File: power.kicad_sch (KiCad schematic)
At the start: 71 parts, among them SW1 SW_Push, U3 BD71847MWV, Y1 Crystal

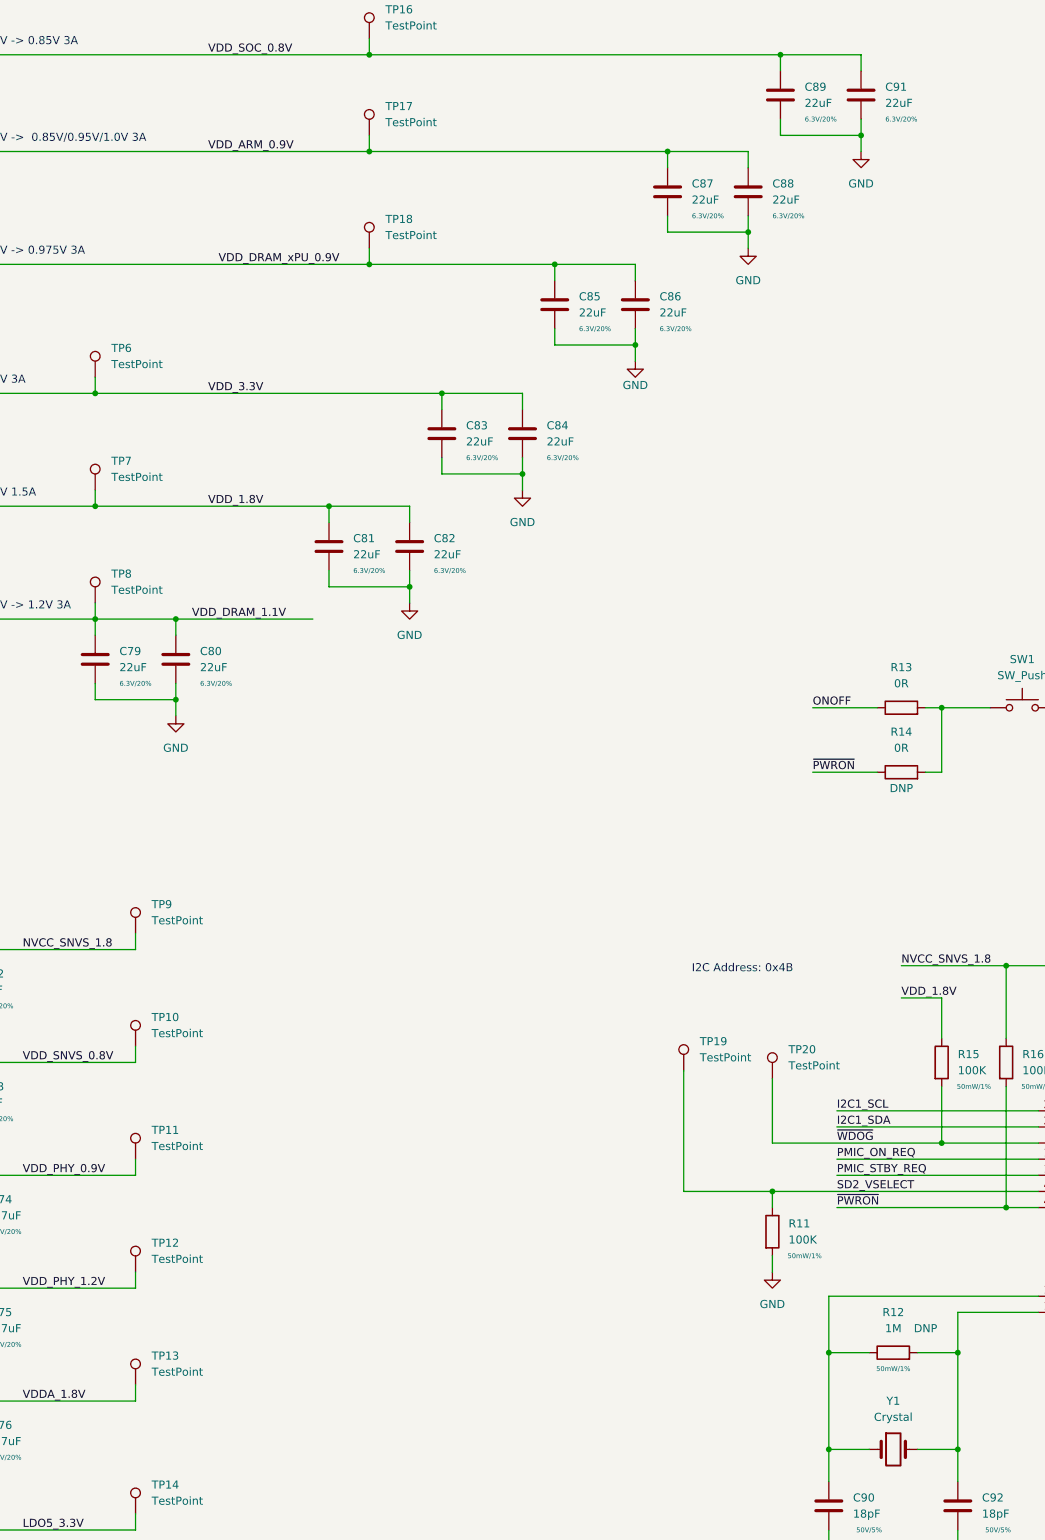
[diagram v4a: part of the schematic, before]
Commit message: bom work, change uart level shifter and m.2 socket
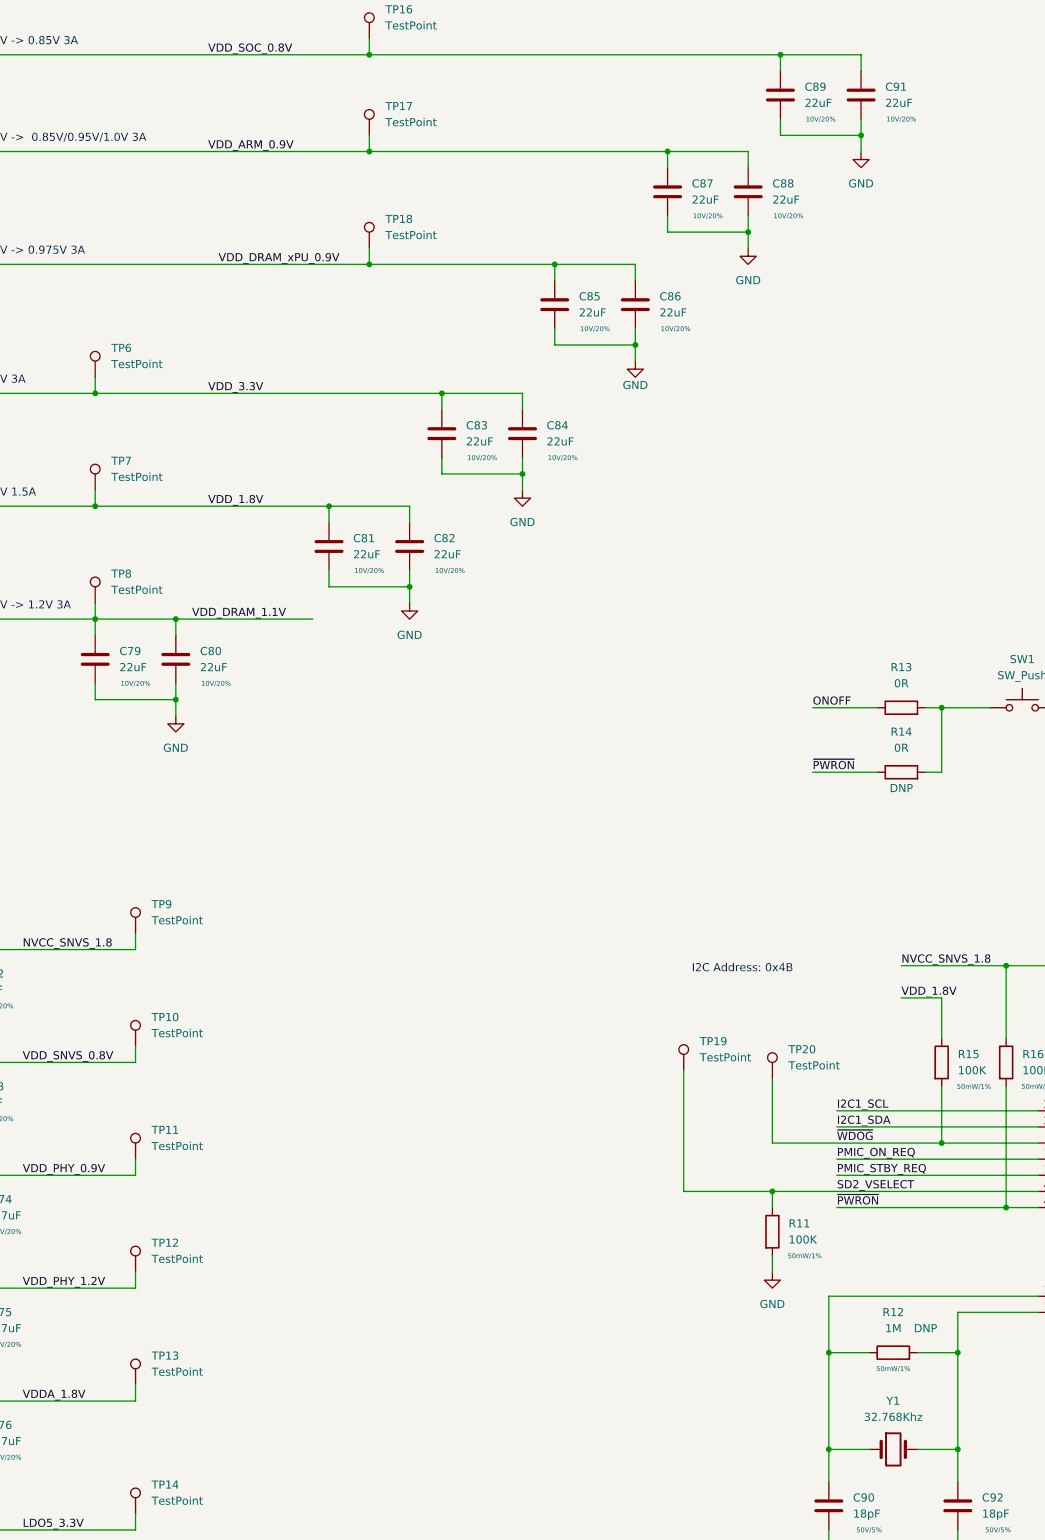
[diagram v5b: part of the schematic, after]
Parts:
- C58, C59, C60: MPN (none) -> GRM155C81C225ME15D
- C61, C62, C63, C74, C75, C76, C77: MPN (none) -> CL05A475MP5NRNC
- C64, C65, C66, C67, C68, C69, C70, C71, C78: MPN (none) -> CL10A106KP8NNNC
- C72, C73, C93, C94: MPN (none) -> CL05A105KP5NNNC
- C79, C80, C81, C82, C83, C84, C85, C86, C87, C88, C89, C91: MPN (none) -> CL10A226MP8NUNE; Rating 6.3V/20% -> 10V/20%
- C90, C92: footprint qsbc:C_0402_1005Metric -> qsbc:C_0201_0603Metric; MPN (none) -> GRM0335C1H180JA01D
- L1, L2, L3, L5, L6: MPN (none) -> DFE252012P-R47M=P2
- L4: MPN (none) -> DFE252012P-1R0M=P2
- R11, R15, R16: MPN (none) -> RC0402FR-07100KL
- R12: MPN (none) -> RC0402FR-071ML
- R13, R14: MPN (none) -> RC0402FR-070RL
- SW1: MPN (none) -> EVQ-P7A01P
- U3: MPN (none) -> BD71847AMWV-E2
- Y1: value Crystal -> 32.768Khz; MPN (none) -> ECS-.327-12.5-12R-C-TR

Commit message: ddr length matching work, misc cleanup
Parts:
- renumbered C58 to C57, C59 to C58, C60 to C59, C61 to C60, C62 to C61, C63 to C62, C64 to C63, C65 to C64, C66 to C65, C67 to C66, C68 to C67, C69 to C68, C70 to C69, C71 to C70, C72 to C71, C73 to C72, C74 to C73, C75 to C74, C76 to C75, C77 to C76, C78 to C77, C79 to C78, C80 to C79, C81 to C80, C82 to C81, C83 to C82, C84 to C83, C85 to C84, C86 to C85, C87 to C86, C88 to C87, C89 to C88, C90 to C89, C91 to C90, C92 to C91, C93 to C92, C94 to C93

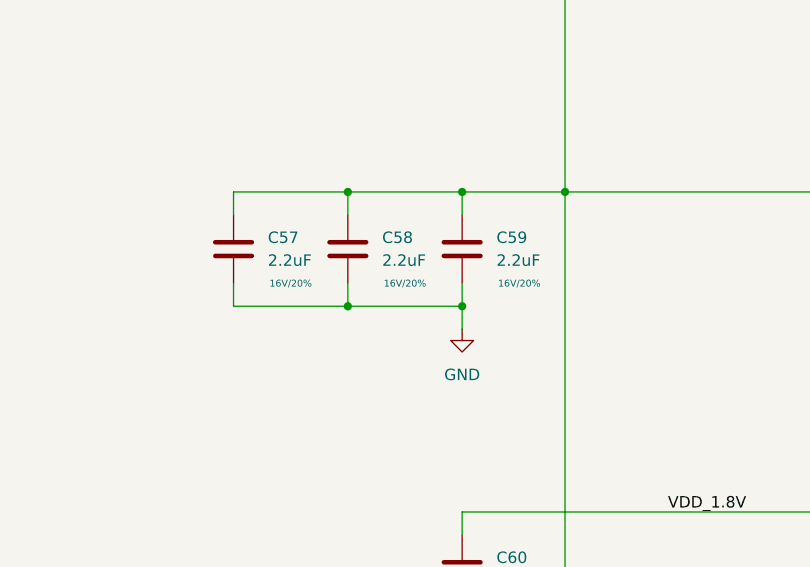
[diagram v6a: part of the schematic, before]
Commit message: misc cleanup, change from usb mux to dual uart
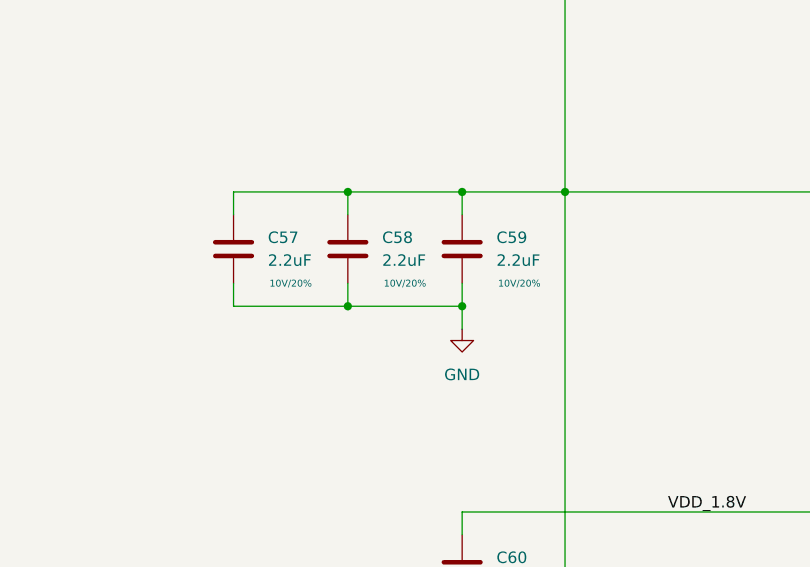
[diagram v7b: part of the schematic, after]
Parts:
- C57, C58, C59: MPN GRM155C81C225ME15D -> GRM155R61A225KE95D; Rating 16V/20% -> 10V/20%
- TP10, TP11, TP12, TP13, TP14, TP15, TP16, TP17, TP18, TP19, TP2, TP20, TP3, TP4, TP5, TP6, TP7, TP8, TP9: now left out of the parts list
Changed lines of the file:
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@@
   )
   (symbol (lib_id "Connector:TestPoint") (at 257.81 49.53 0) (unit 1)
-    (in_bom yes) (on_board yes) (fields_autoplaced)
+    (in_bom no) (on_board yes) (fields_autoplaced)
     (property "Reference" "TP16" (id 0) (at 260.35 44.9579 0)
       (effects (font (size 1.27 1.27)) (justify left))
@@
   )
   (symbol (lib_id "Connector:TestPoint") (at 73.66 381 0) (unit 1)
-    (in_bom yes) (on_board yes) (fields_autoplaced)
+    (in_bom no) (on_board yes) (fields_autoplaced)
     (property "Reference" "TP4" (id 0) (at 76.2 376.4279 0)
       (effects (font (size 1.27 1.27)) (justify left))
@@
   )
   (symbol (lib_id "Connector:TestPoint") (at 220.98 281.94 0) (unit 1)
-    (in_bom yes) (on_board yes) (fields_autoplaced)
+    (in_bom no) (on_board yes) (fields_autoplaced)
     (property "Reference" "TP14" (id 0) (at 223.52 277.3679 0)
       (effects (font (size 1.27 1.27)) (justify left))
@@
   )
   (symbol (lib_id "Connector:TestPoint") (at 220.98 226.06 0) (unit 1)
-    (in_bom yes) (on_board yes) (fields_autoplaced)
+    (in_bom no) (on_board yes) (fields_autoplaced)
     (property "Reference" "TP11" (id 0) (at 223.52 221.4879 0)
       (effects (font (size 1.27 1.27)) (justify left))
@@
   )
   (symbol (lib_id "Connector:TestPoint") (at 59.69 381 0) (unit 1)
-    (in_bom yes) (on_board yes) (fields_autoplaced)
+    (in_bom no) (on_board yes) (fields_autoplaced)
     (property "Reference" "TP3" (id 0) (at 62.23 376.4279 0)
       (effects (font (size 1.27 1.27)) (justify left))
@@
       (effects (font (size 1.27 1.27)) hide)
     )
-    (property "Rating" "16V/20%" (id 4) (at 77.47 203.2 0)
-      (effects (font (size 0.762 0.762)))
-    )
-    (property "MPN" "GRM155C81C225ME15D" (id 5) (at 71.12 199.39 0)
+    (property "Rating" "10V/20%" (id 4) (at 77.47 203.2 0)
+      (effects (font (size 0.762 0.762)))
+    )
+    (property "MPN" "GRM155R61A225KE95D" (id 5) (at 71.12 199.39 0)
       (effects (font (size 1.27 1.27)) hide)
     )
@@
   )
   (symbol (lib_id "Connector:TestPoint") (at 45.72 381 0) (unit 1)
-    (in_bom yes) (on_board yes) (fields_autoplaced)
+    (in_bom no) (on_board yes) (fields_autoplaced)
     (property "Reference" "TP2" (id 0) (at 48.26 376.4279 0)
       (effects (font (size 1.27 1.27)) (justify left))
@@
   )
   (symbol (lib_id "Connector:TestPoint") (at 220.98 299.72 0) (unit 1)
-    (in_bom yes) (on_board yes) (fields_autoplaced)
+    (in_bom no) (on_board yes) (fields_autoplaced)
     (property "Reference" "TP15" (id 0) (at 223.52 295.1479 0)
       (effects (font (size 1.27 1.27)) (justify left))
@@
   )
   (symbol (lib_id "Connector:TestPoint") (at 214.63 102.87 0) (unit 1)
-    (in_bom yes) (on_board yes) (fields_autoplaced)
+    (in_bom no) (on_board yes) (fields_autoplaced)
     (property "Reference" "TP6" (id 0) (at 217.17 98.2979 0)
       (effects (font (size 1.27 1.27)) (justify left))
@@
       (effects (font (size 1.27 1.27)) hide)
     )
-    (property "Rating" "16V/20%" (id 4) (at 64.77 203.2 0)
-      (effects (font (size 0.762 0.762)))
-    )
-    (property "MPN" "GRM155C81C225ME15D" (id 5) (at 58.42 199.39 0)
+    (property "Rating" "10V/20%" (id 4) (at 64.77 203.2 0)
+      (effects (font (size 0.762 0.762)))
+    )
+    (property "MPN" "GRM155R61A225KE95D" (id 5) (at 58.42 199.39 0)
       (effects (font (size 1.27 1.27)) hide)
     )
@@
   )
   (symbol (lib_id "Connector:TestPoint") (at 257.81 82.55 0) (unit 1)
-    (in_bom yes) (on_board yes) (fields_autoplaced)
+    (in_bom no) (on_board yes) (fields_autoplaced)
     (property "Reference" "TP18" (id 0) (at 260.35 77.9779 0)
       (effects (font (size 1.27 1.27)) (justify left))
@@
   )
   (symbol (lib_id "Connector:TestPoint") (at 220.98 261.62 0) (unit 1)
-    (in_bom yes) (on_board yes) (fields_autoplaced)
+    (in_bom no) (on_board yes) (fields_autoplaced)
     (property "Reference" "TP13" (id 0) (at 223.52 257.0479 0)
       (effects (font (size 1.27 1.27)) (justify left))
@@
   )
   (symbol (lib_id "Connector:TestPoint") (at 220.98 190.5 0) (unit 1)
-    (in_bom yes) (on_board yes) (fields_autoplaced)
+    (in_bom no) (on_board yes) (fields_autoplaced)
     (property "Reference" "TP9" (id 0) (at 223.52 185.9279 0)
       (effects (font (size 1.27 1.27)) (justify left))
@@
   )
   (symbol (lib_id "Connector:TestPoint") (at 214.63 120.65 0) (unit 1)
-    (in_bom yes) (on_board yes) (fields_autoplaced)
+    (in_bom no) (on_board yes) (fields_autoplaced)
     (property "Reference" "TP7" (id 0) (at 217.17 116.0779 0)
       (effects (font (size 1.27 1.27)) (justify left))
@@
       (effects (font (size 1.27 1.27)) hide)
     )
-    (property "Rating" "16V/20%" (id 4) (at 90.17 203.2 0)
-      (effects (font (size 0.762 0.762)))
-    )
-    (property "MPN" "GRM155C81C225ME15D" (id 5) (at 83.82 199.39 0)
+    (property "Rating" "10V/20%" (id 4) (at 90.17 203.2 0)
+      (effects (font (size 0.762 0.762)))
+    )
+    (property "MPN" "GRM155R61A225KE95D" (id 5) (at 83.82 199.39 0)
       (effects (font (size 1.27 1.27)) hide)
     )
@@
   )
   (symbol (lib_id "Connector:TestPoint") (at 257.81 64.77 0) (unit 1)
-    (in_bom yes) (on_board yes) (fields_autoplaced)
+    (in_bom no) (on_board yes) (fields_autoplaced)
     (property "Reference" "TP17" (id 0) (at 260.35 60.1979 0)
       (effects (font (size 1.27 1.27)) (justify left))
@@
   )
   (symbol (lib_id "Connector:TestPoint") (at 220.98 208.28 0) (unit 1)
-    (in_bom yes) (on_board yes) (fields_autoplaced)
+    (in_bom no) (on_board yes) (fields_autoplaced)
     (property "Reference" "TP10" (id 0) (at 223.52 203.7079 0)
       (effects (font (size 1.27 1.27)) (justify left))
@@
   )
   (symbol (lib_id "Connector:TestPoint") (at 87.63 381 0) (unit 1)
-    (in_bom yes) (on_board yes) (fields_autoplaced)
+    (in_bom no) (on_board yes) (fields_autoplaced)
     (property "Reference" "TP5" (id 0) (at 90.17 376.4279 0)
       (effects (font (size 1.27 1.27)) (justify left))
@@
   )
   (symbol (lib_id "Connector:TestPoint") (at 220.98 243.84 0) (unit 1)
-    (in_bom yes) (on_board yes) (fields_autoplaced)
+    (in_bom no) (on_board yes) (fields_autoplaced)
     (property "Reference" "TP12" (id 0) (at 223.52 239.2679 0)
       (effects (font (size 1.27 1.27)) (justify left))
@@
   )
   (symbol (lib_id "Connector:TestPoint") (at 307.34 212.09 0) (unit 1)
-    (in_bom yes) (on_board yes) (fields_autoplaced)
+    (in_bom no) (on_board yes) (fields_autoplaced)
     (property "Reference" "TP19" (id 0) (at 309.88 207.5179 0)
       (effects (font (size 1.27 1.27)) (justify left))
@@
   )
   (symbol (lib_id "Connector:TestPoint") (at 321.31 213.36 0) (unit 1)
-    (in_bom yes) (on_board yes) (fields_autoplaced)
+    (in_bom no) (on_board yes) (fields_autoplaced)
     (property "Reference" "TP20" (id 0) (at 323.85 208.7879 0)
       (effects (font (size 1.27 1.27)) (justify left))
@@
   )
   (symbol (lib_id "Connector:TestPoint") (at 214.63 138.43 0) (unit 1)
-    (in_bom yes) (on_board yes) (fields_autoplaced)
+    (in_bom no) (on_board yes) (fields_autoplaced)
     (property "Reference" "TP8" (id 0) (at 217.17 133.8579 0)
       (effects (font (size 1.27 1.27)) (justify left))

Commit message: Rev 1
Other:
- note added: "1.1V 3A"
- note removed: "1.1V -> 1.2V 3A"
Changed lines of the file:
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@@
   (title_block
     (title "QSBC")
-    (rev "1")
+    (date "2022-12-01")
+    (rev "1.0")
     (company "Q-LAB")
   )
@@
     (effects (font (size 1.27 1.27)) (justify left bottom))
   )
-  (text "1.1V -> 1.2V 3A\n" (at 196.85 139.7 0)
+  (text "1.1V 3A\n" (at 196.85 139.7 0)
     (effects (font (size 1.27 1.27)) (justify left bottom))
   )
